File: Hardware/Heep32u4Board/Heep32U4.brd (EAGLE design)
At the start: 65 x 45 mm, 59 parts, among them J2 AVR_SPI_PROG_3X2PTH, J4 MAGJACK, K1 RELAY-SPDT-JZC-11F, K2 RELAY-SPDT-JZC-11F, Q1 25MHz, Q2 5.8A/30V/35mΩ, Q3 5.8A/30V/35mΩ, U1 +3.3v, U2 ENC28J60-SO, Y1 16MHz

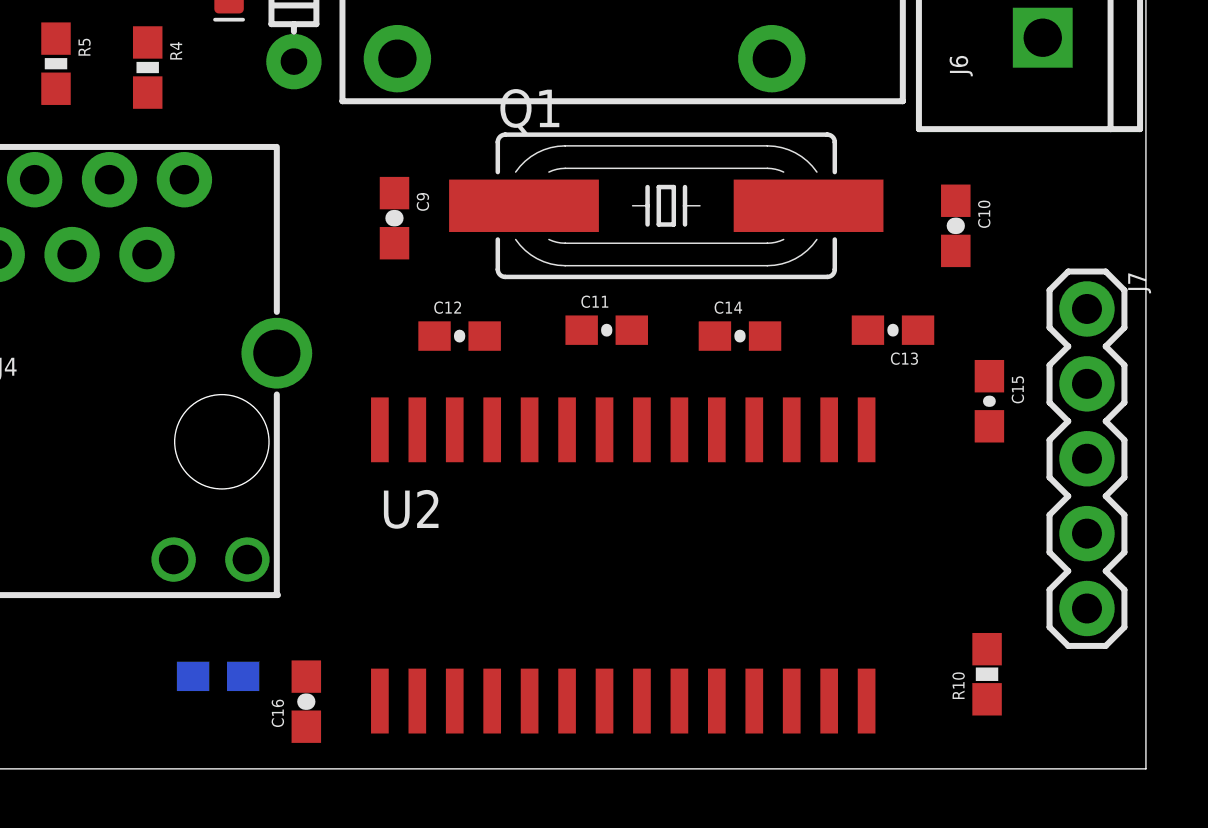
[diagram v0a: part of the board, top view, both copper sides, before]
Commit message: #20 Rearranged some resistors
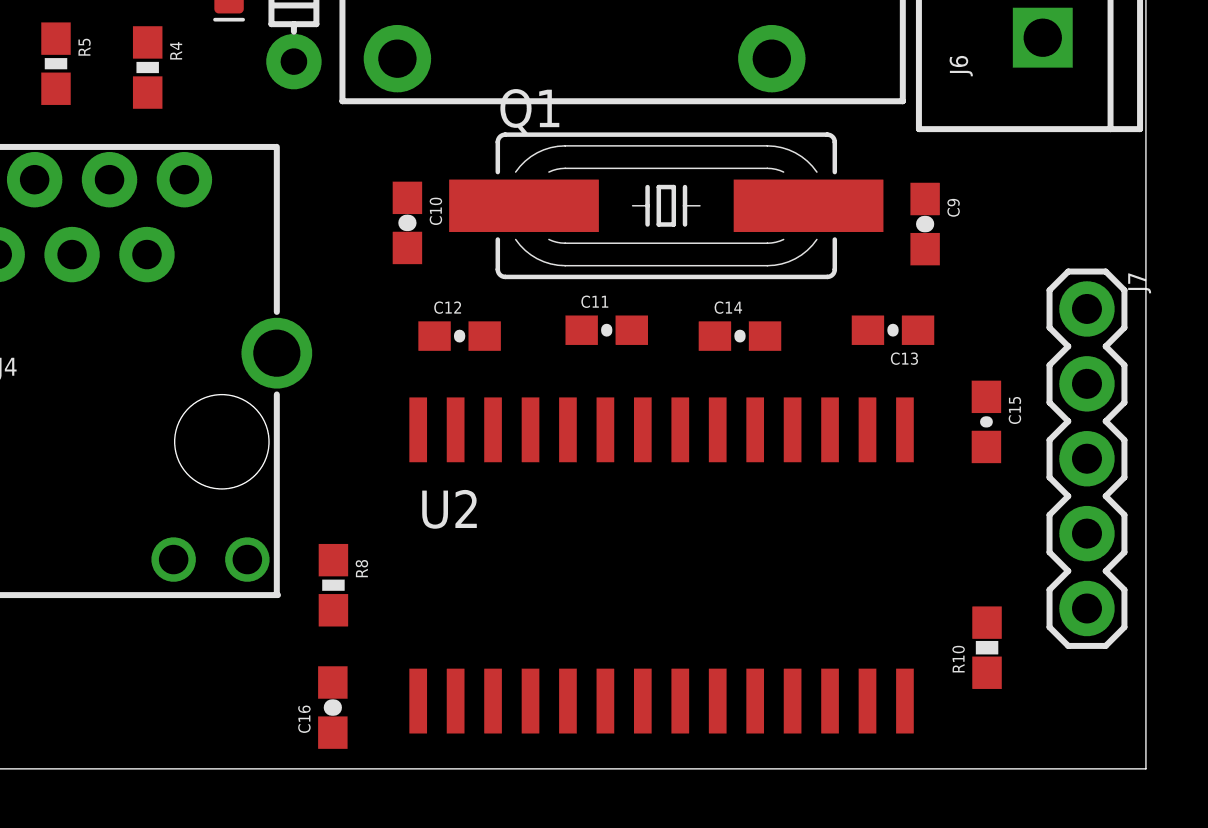
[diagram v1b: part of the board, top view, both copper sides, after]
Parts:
- moved C10 18.6 mm to (40.0, 18.5)
- moved C9 18.0 mm to (57.5, 18.5)
- moved R8 4.98 mm to (37.4, 6.23), flipped to the top, turned to 270 degrees
- moved U2 1.30 mm to (48.6, 6.90)
- moved C16 0.92 mm to (37.4, 2.08)
- moved R10 0.90 mm to (59.6, 4.11)
- moved C15 0.71 mm to (59.6, 11.8)

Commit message: #20 Board final layout
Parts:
- moved J3 2.73 mm to (13.8, 2.26), turned to 0 degrees
- moved C8 1.20 mm to (25.8, 27.3)
- moved C1 1.08 mm to (16.2, 15.6)
- moved R4 0.85 mm to (31.1, 22.9), turned to 0 degrees
- moved Y1 0.22 mm to (11.6, 20.4)
- moved J2 0.22 mm to (2.44, 30.7)
- moved R9 0.22 mm to (17.5, 7.24)
- moved C7 0.22 mm to (29.7, 29.6)
- moved C17 0.20 mm to (15.4, 16.5)
- moved L1 0.20 mm to (29.7, 27.1)
- moved R11 0.10 mm to (26.3, 32.0)
- moved S2 0.10 mm to (25.2, 41.3)

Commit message: #20 Begin routing ATMega32U4 board
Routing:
- net 3.3V: track 0.00 -> 85.1 mm, vias 0 -> 3
- net VOUT: track 0.00 -> 63.9 mm, vias 0 -> 2
- net RD-: track 0.00 -> 41.7 mm, vias 0 -> 2
- net RD+: track 0.00 -> 40.8 mm, vias 0 -> 2
- net V_USB: track 0.00 -> 38.4 mm, vias 0 -> 1
- net RESET: track 0.00 -> 30.9 mm
- net SCK: track 0.00 -> 26.5 mm, vias 0 -> 1
- net SO: track 0.00 -> 23.5 mm, vias 0 -> 2
- net GND: track 0.00 -> 22.6 mm, vias 0 -> 5
- net SI: track 0.00 -> 22.3 mm, vias 0 -> 1
- net N$10: track 0.00 -> 18.0 mm
- net N$9: track 0.00 -> 14.1 mm
- net VIN: track 0.00 -> 11.7 mm
- net N$4: track 0.00 -> 5.72 mm
- net N$15: track 0.00 -> 4.07 mm
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- added copper zone on layer 1, net GND
- added copper zone on layer 16, net GND

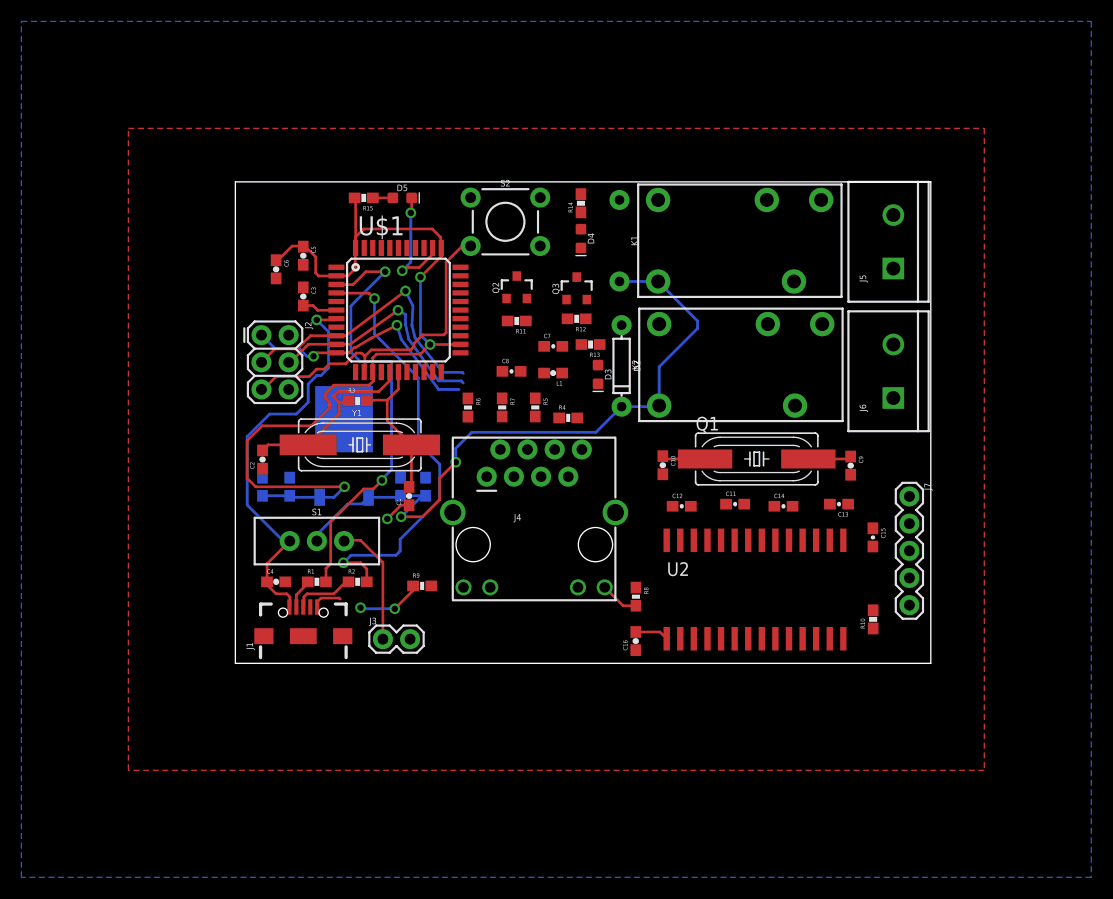
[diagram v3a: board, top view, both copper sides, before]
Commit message: #20 Fully routed ATMegaBoard
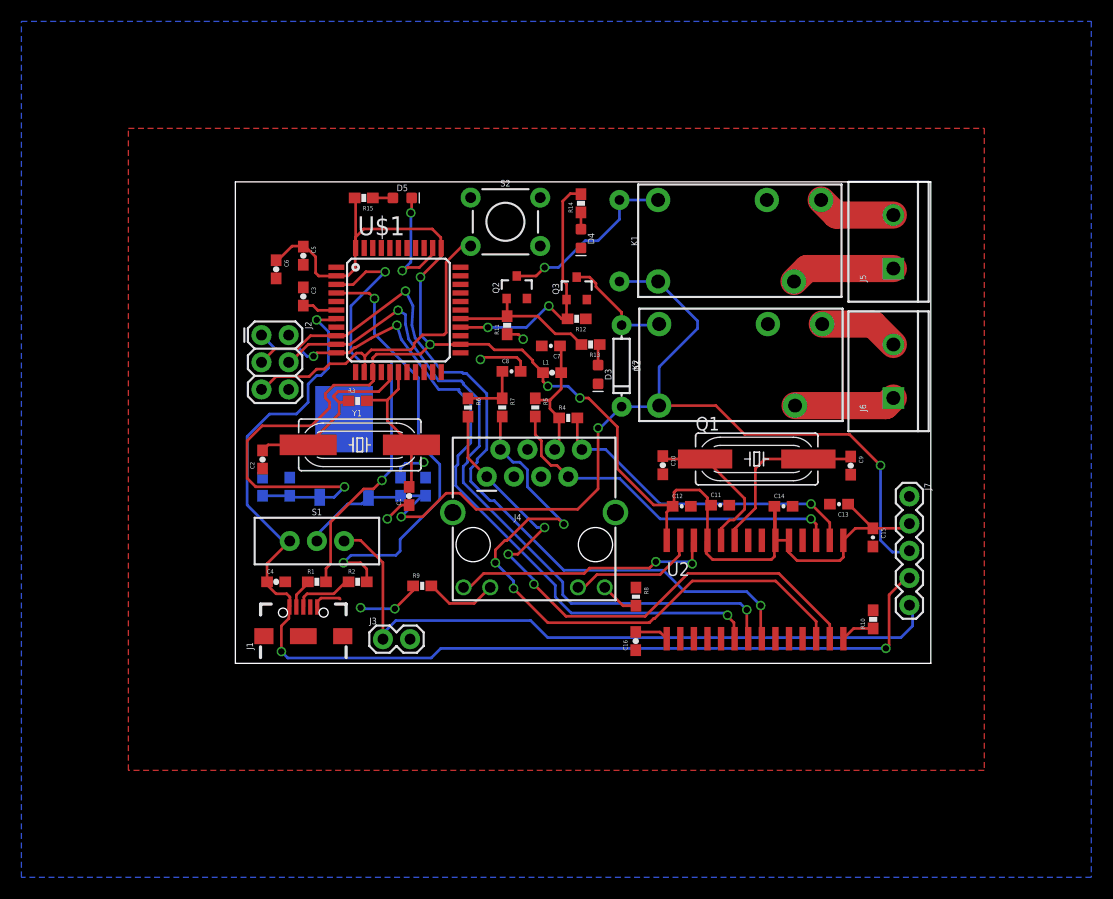
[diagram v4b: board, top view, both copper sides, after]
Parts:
- moved C11 1.40 mm to (45.3, 14.8)
- moved R11 0.98 mm to (25.4, 31.6), turned to 90 degrees
- moved C7 0.22 mm to (29.5, 29.7), turned to 180 degrees
- moved L1 0.11 mm to (29.6, 27.2), turned to 0 degrees
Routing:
- net 3.3V: track 85.1 -> 162.4 mm, vias 3 -> 5
- net V_USB: track 38.4 -> 107.7 mm, vias 1 -> 3
- net N$5: track 0.00 -> 59.5 mm, vias 0 -> 3
- net N$2: track 0.00 -> 55.8 mm, vias 0 -> 3
- net VIN: track 11.7 -> 65.4 mm
- net SCK: track 26.5 -> 73.4 mm, vias 1 -> 2
- net SI: track 22.3 -> 67.7 mm, vias 1 -> 2
- net SO: track 23.5 -> 67.0 mm, vias 2 -> 3
- net VOUT: track 63.9 -> 99.8 mm, vias 2 -> 3
- net N$7: track 0.00 -> 33.8 mm, vias 0 -> 1
- net N$6: track 0.00 -> 30.8 mm, vias 0 -> 1
- net LEDB: track 0.00 -> 24.7 mm, vias 0 -> 2
- net RELAY2: track 0.00 -> 24.5 mm, vias 0 -> 2
- net N$23: track 0.00 -> 17.2 mm, vias 0 -> 1
- net RELAY1: track 0.00 -> 14.2 mm
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
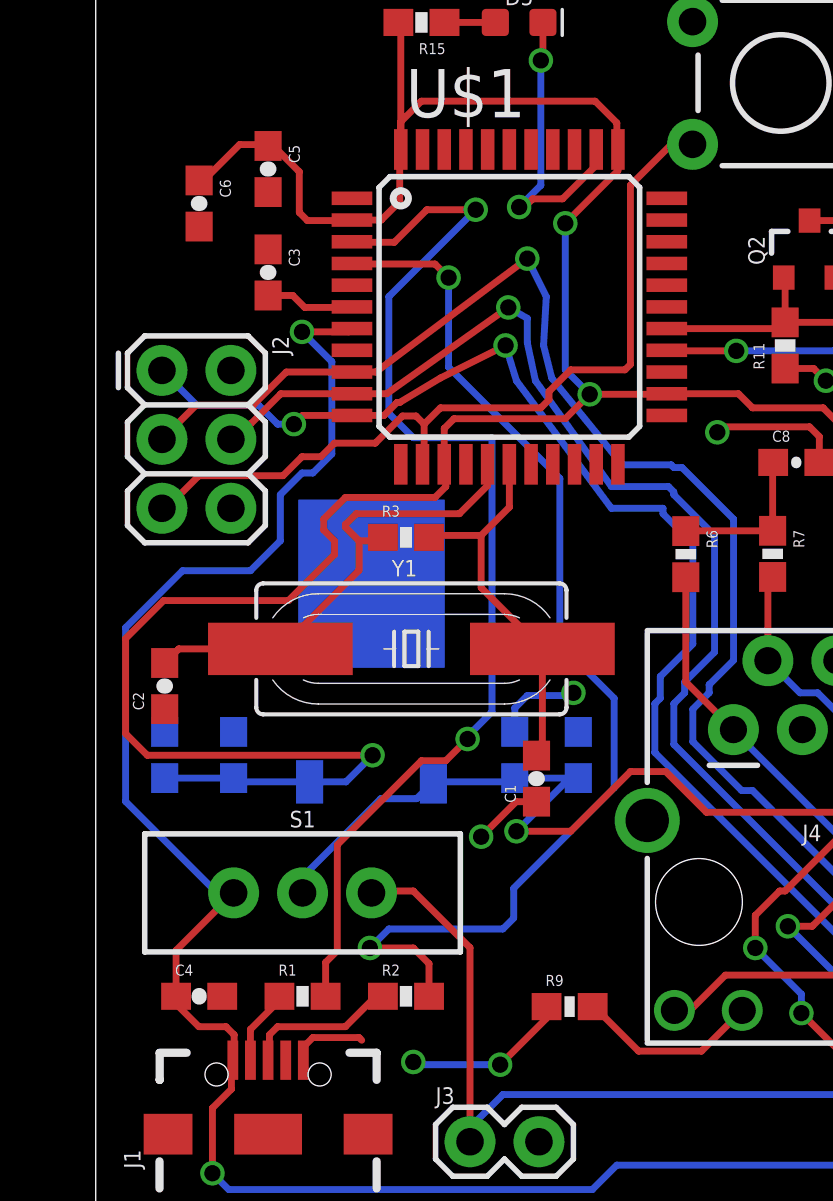
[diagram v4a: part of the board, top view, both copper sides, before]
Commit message: #20 Cleared all DRC errors
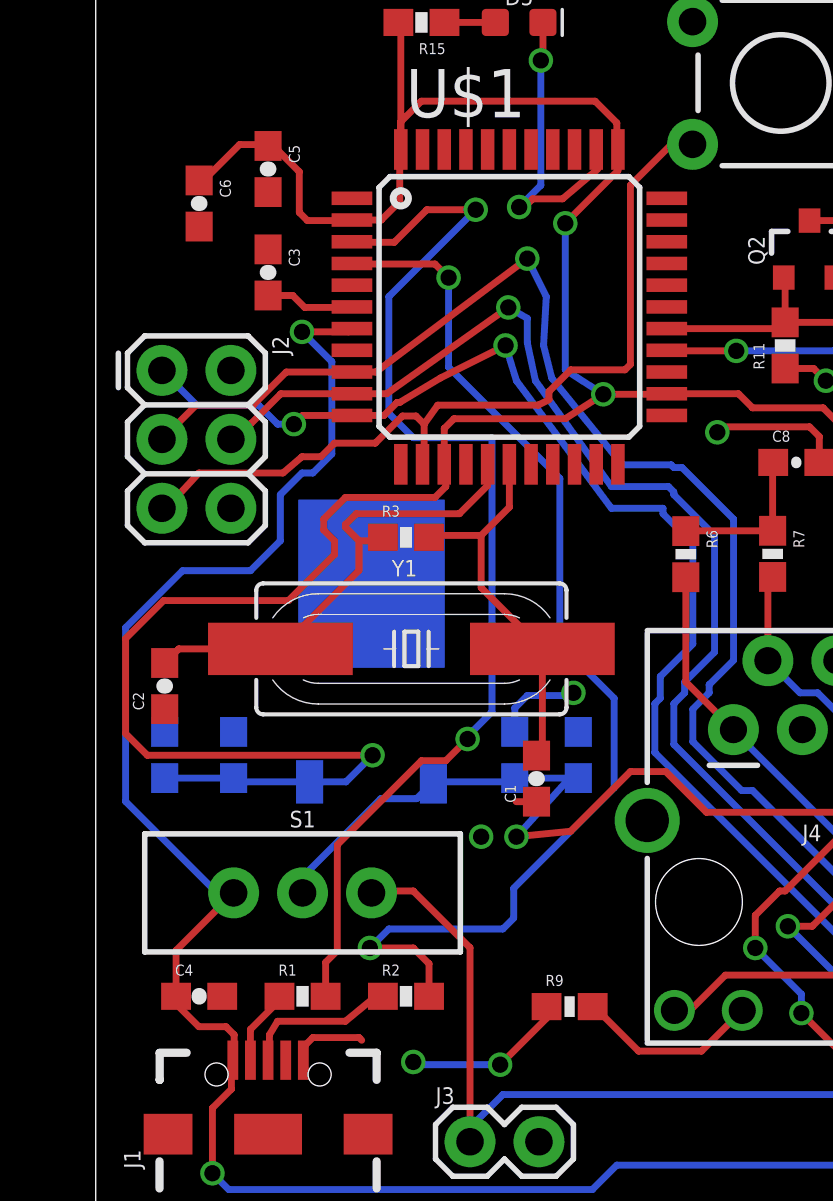
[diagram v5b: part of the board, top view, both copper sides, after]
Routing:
- net GND: track 33.1 -> 31.2 mm
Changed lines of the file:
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@@
 <contactref element="R2" pad="1"/>
 <wire x1="10.58" y1="7.62" x2="10.32" y2="7.62" width="0.254" layer="1"/>
-<wire x1="10.32" y1="7.62" x2="9.2" y2="6.5" width="0.254" layer="1"/>
-<wire x1="9.2" y1="6.5" x2="6.7" y2="6.5" width="0.254" layer="1"/>
-<wire x1="6.7" y1="6.5" x2="6.4" y2="6.2" width="0.254" layer="1"/>
+<wire x1="10.32" y1="7.62" x2="9.2" y2="6.7" width="0.254" layer="1"/>
+<wire x1="9.2" y1="6.7" x2="6.7" y2="6.7" width="0.254" layer="1"/>
+<wire x1="6.7" y1="6.7" x2="6.4" y2="6.2" width="0.254" layer="1"/>
 <wire x1="6.4" y1="6.2" x2="6.4" y2="5.315" width="0.254" layer="1"/>
 <wire x1="6.4" y1="5.315" x2="6.35" y2="5.265" width="0.254" layer="1"/>
@@
 <wire x1="9.7" y1="6.1" x2="9.8" y2="6" width="0.254" layer="1"/>
 <wire x1="16.24" y1="14.79" x2="15.49" y2="14.79" width="0.254" layer="1"/>
-<wire x1="15.49" y1="14.79" x2="14.2" y2="13.5" width="0.254" layer="1"/>
 <via x="14.2" y="13.5" extent="1-16" drill="0.6" shape="square"/>
 <wire x1="14.2" y1="13.5" x2="14" y2="13.5" width="0.254" layer="16"/>
@@
 <wire x1="15.8" y1="36.7" x2="16.1" y2="37" width="0.254" layer="1"/>
 <wire x1="16.1" y1="37" x2="17.2" y2="37" width="0.254" layer="1"/>
-<wire x1="17.2" y1="37" x2="18.4" y2="38.2" width="0.254" layer="1"/>
+<wire x1="17.2" y1="37" x2="18.5" y2="38.1" width="0.254" layer="1"/>
 <wire x1="26.66" y1="27.29" x2="26.66" y2="28.24" width="0.254" layer="1"/>
 <wire x1="26.66" y1="28.24" x2="26.3" y2="28.6" width="0.254" layer="1"/>
@@
 <contactref element="S2" pad="3"/>
 <wire x1="2.44" y1="25.6" x2="2.6" y2="25.6" width="0.254" layer="1"/>
-<wire x1="2.6" y1="25.6" x2="3.8" y2="26.8" width="0.254" layer="1"/>
-<wire x1="3.8" y1="26.8" x2="6.9" y2="26.8" width="0.254" layer="1"/>
-<wire x1="6.9" y1="26.8" x2="7.6" y2="27.5" width="0.254" layer="1"/>
+<wire x1="2.6" y1="25.6" x2="3.8" y2="26.9" width="0.254" layer="1"/>
+<wire x1="3.8" y1="26.9" x2="6.9" y2="26.9" width="0.254" layer="1"/>
+<wire x1="6.9" y1="26.9" x2="7.6" y2="27.5" width="0.254" layer="1"/>
 <wire x1="7.6" y1="27.5" x2="8.3" y2="27.5" width="0.254" layer="1"/>
 <wire x1="8.3" y1="27.5" x2="8.8" y2="28" width="0.254" layer="1"/>
@@
 <wire x1="17.5" y1="30.7" x2="16.7" y2="29.9" width="0.254" layer="1"/>
 <wire x1="16.7" y1="29.9" x2="16.7" y2="29.6" width="0.254" layer="1"/>
-<wire x1="16.7" y1="29.6" x2="16.4" y2="29.3" width="0.254" layer="1"/>
-<wire x1="16.4" y1="29.3" x2="12.7" y2="29.3" width="0.254" layer="1"/>
-<wire x1="12.7" y1="29.3" x2="12.1" y2="28.7" width="0.254" layer="1"/>
+<wire x1="16.7" y1="29.6" x2="16.3" y2="29.4" width="0.254" layer="1"/>
+<wire x1="16.3" y1="29.4" x2="12.6" y2="29.4" width="0.254" layer="1"/>
+<wire x1="12.6" y1="29.4" x2="12.1" y2="28.7" width="0.254" layer="1"/>
 </signal>
 <signal name="N$2">
@@
 <via x="17.3" y="36.1" extent="1-16" drill="0.6" shape="square"/>
 <wire x1="17.3" y1="36.1" x2="17.3" y2="30.7" width="0.254" layer="16"/>
-<wire x1="17.3" y1="30.7" x2="18.2" y2="29.8" width="0.254" layer="16"/>
-<via x="18.2" y="29.8" extent="1-16" drill="0.6" shape="square"/>
-<wire x1="18.2" y1="29.8" x2="21.02" y2="29.8" width="0.254" layer="1"/>
+<wire x1="17.3" y1="30.7" x2="18.7" y2="29.8" width="0.254" layer="16"/>
+<via x="18.7" y="29.8" extent="1-16" drill="0.6" shape="square"/>
+<wire x1="18.7" y1="29.8" x2="21.02" y2="29.8" width="0.254" layer="1"/>
 <wire x1="21.02" y1="29.8" x2="21.04" y2="29.82" width="0.254" layer="1"/>
 <wire x1="12.84" y1="27.22" x2="12.84" y2="28.54" width="0.254" layer="1"/>
 <wire x1="12.84" y1="28.54" x2="13.2" y2="28.9" width="0.254" layer="1"/>
 <wire x1="13.2" y1="28.9" x2="17.3" y2="28.9" width="0.254" layer="1"/>
-<wire x1="17.3" y1="28.9" x2="18.2" y2="29.8" width="0.254" layer="1"/>
+<wire x1="17.3" y1="28.9" x2="18.7" y2="29.8" width="0.254" layer="1"/>
 <wire x1="21.04" y1="29.82" x2="23.68" y2="29.82" width="0.254" layer="1"/>
 <wire x1="23.68" y1="29.82" x2="24.2" y2="29.3" width="0.254" layer="1"/>
@@
 <wire x1="15.44" y1="15.66" x2="17.78" y2="15.66" width="0.254" layer="16"/>
 <wire x1="17.78" y1="15.66" x2="17.46" y2="15.66" width="0.254" layer="16"/>
-<wire x1="17.46" y1="15.66" x2="15.5" y2="13.7" width="0.254" layer="16"/>
-<via x="15.5" y="13.7" extent="1-16" drill="0.6" shape="square"/>
-<wire x1="15.5" y1="13.7" x2="17.5" y2="13.7" width="0.254" layer="1"/>
+<wire x1="17.46" y1="15.66" x2="15.5" y2="13.5" width="0.254" layer="16"/>
+<via x="15.5" y="13.5" extent="1-16" drill="0.6" shape="square"/>
+<wire x1="15.5" y1="13.5" x2="17.5" y2="13.7" width="0.254" layer="1"/>
 <wire x1="17.5" y1="13.7" x2="19.7" y2="15.9" width="0.254" layer="1"/>
 <wire x1="36.1" y1="23.99" x2="39.51" y2="23.99" width="0.254" layer="16"/>
@@
 </signal>
 </signals>
+<errors>
+</errors>
 </board>
 </drawing>
